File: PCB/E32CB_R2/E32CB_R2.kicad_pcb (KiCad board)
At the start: 2 copper layers, 111.3 x 90.9 mm, 89 parts, among them J1 GPIO_HEADER, J10 S, J11 Q4, J12 S, J13 Q3, J14 S, J15 Q8, J16 S, J17 Q7, J18 S, J19 Q6, J2 Power, J20 S, J21 Q5, J22 S, J3 USB_B, J4 USB +5V, J5 NEXTION, J6 I2C, J7 Q1, J8 S, J9 Q2, Q1 S8050, Q10 IRLR2905, Q2 S8050, Q3 IRLR2905, Q4 IRLR2905, Q5 IRLR2905, Q6 IRLR2905, Q7 IRLR2905, Q8 IRLR2905, Q9 IRLR2905, U1 ESP32-WROOM-32, X1 12MHz

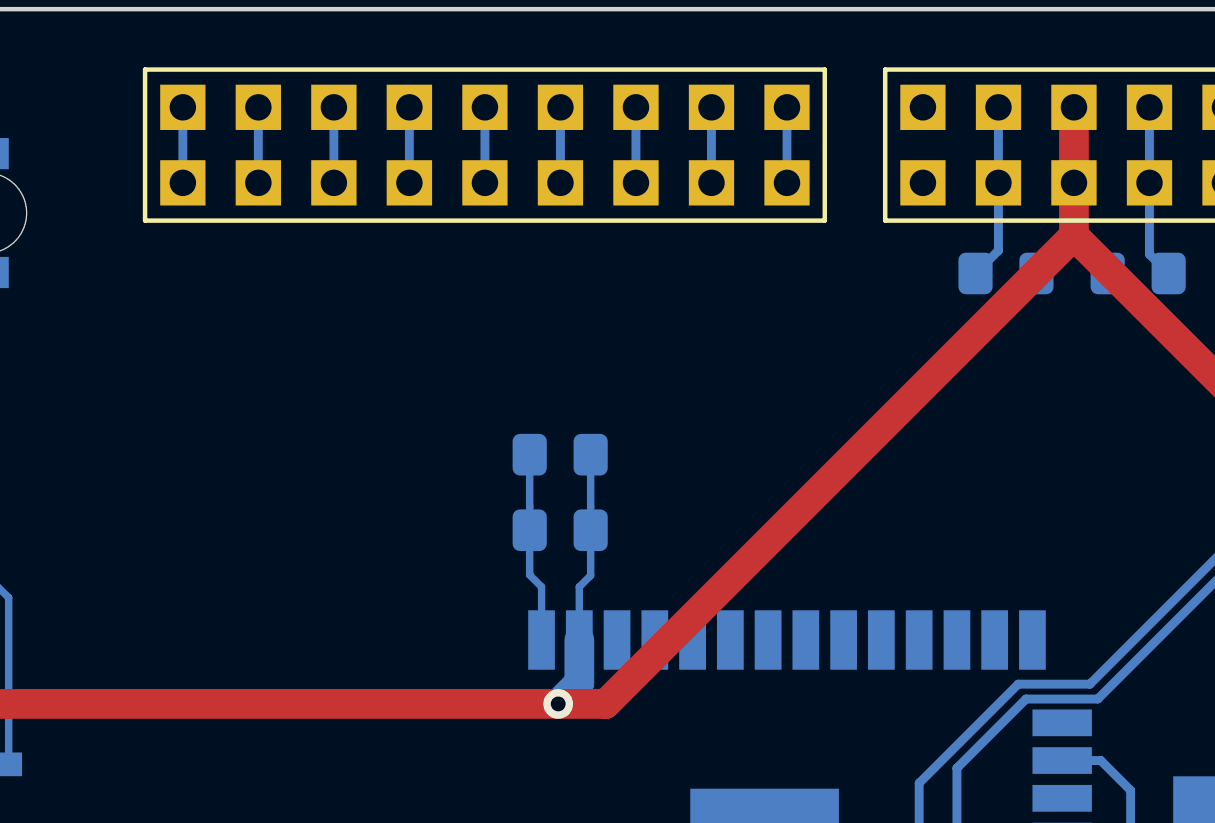
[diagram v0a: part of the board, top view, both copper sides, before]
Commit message: gpio header pins changed
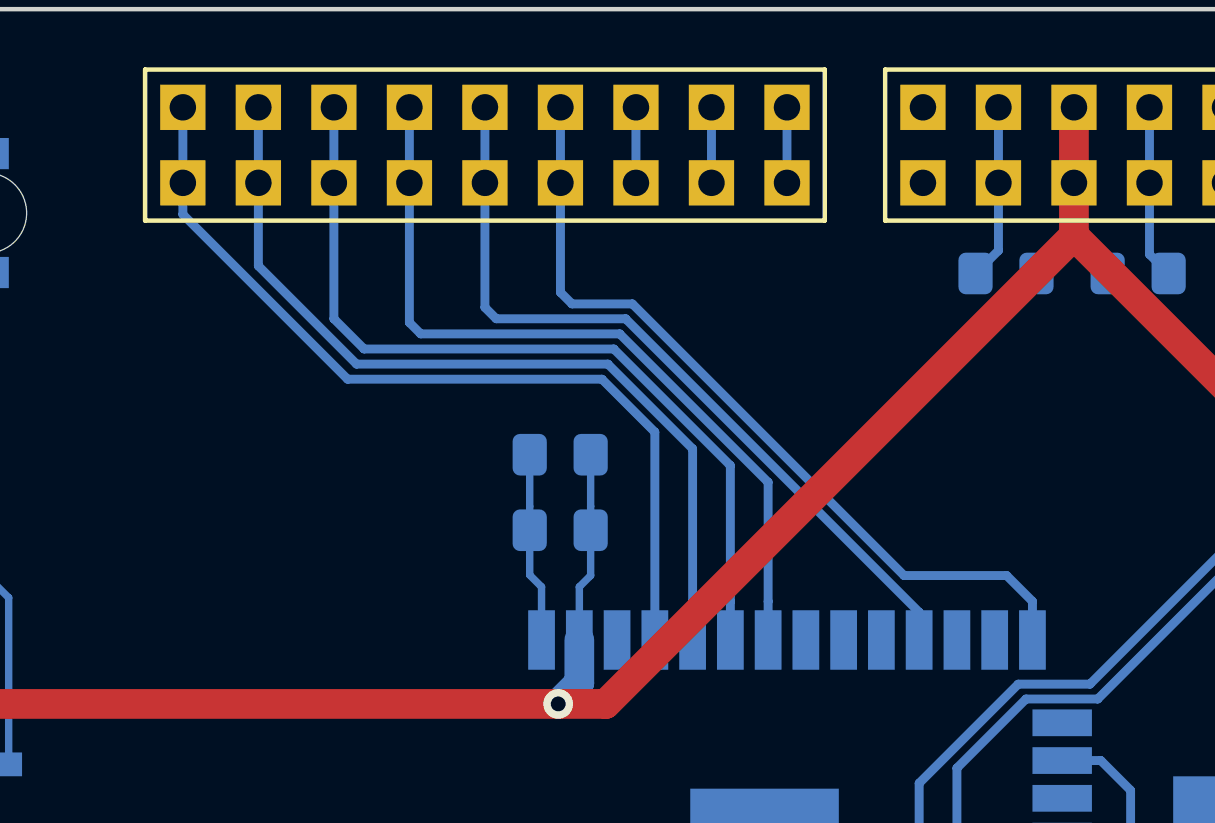
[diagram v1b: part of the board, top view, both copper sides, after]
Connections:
- J1 pad 1: /gpi39 -> /gpi36
- J1 pad 11: /gpio15 -> /gpio12
- J1 pad 12: /gpio15 -> /gpio12
- J1 pad 13: /gpio12 -> /gpio15
- J1 pad 14: /gpio12 -> /gpio15
- J1 pad 2: /gpi39 -> /gpi36
- J1 pad 3: /gpi36 -> /gpi39
- J1 pad 4: /gpi36 -> /gpi39
- J1 pad 5: /gpi35 -> /gpi34
- J1 pad 6: /gpi35 -> /gpi34
- J1 pad 7: /gpi34 -> /gpi35
- J1 pad 8: /gpi34 -> /gpi35
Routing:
- net /gpi36: track 2.54 -> 29.5 mm
- net /gpi39: track 2.54 -> 28.9 mm
- net /gpi34: track 2.54 -> 28.4 mm
- net /gpio12: track 2.54 -> 27.7 mm
- net /gpi35: track 2.54 -> 26.8 mm
- net /gpio26: track 2.54 -> 26.5 mm
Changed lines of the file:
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@@
     (thickness 1.6)
     (drawings 8)
-    (tracks 533)
+    (tracks 568)
     (zones 0)
     (modules 89)
@@
     (fp_line (start -2.54 11.43) (end -2.54 -11.43) (layer F.SilkS) (width 0.15))
     (pad 1 thru_hole rect (at -1.27 -10.16 90) (size 1.524 1.524) (drill 0.889) (layers *.Cu *.Mask F.SilkS)
-      (net 45 /gpi39))
+      (net 44 /gpi36))
     (pad 2 thru_hole rect (at 1.27 -10.16 90) (size 1.524 1.524) (drill 0.889) (layers *.Cu *.Mask F.SilkS)
-      (net 45 /gpi39))
-    (pad 3 thru_hole rect (at -1.27 -7.62 90) (size 1.524 1.524) (drill 0.889) (layers *.Cu *.Mask F.SilkS)
       (net 44 /gpi36))
+    (pad 3 thru_hole rect (at -1.27 -7.62 90) (size 1.524 1.524) (drill 0.889) (layers *.Cu *.Mask F.SilkS)
+      (net 45 /gpi39))
     (pad 4 thru_hole rect (at 1.27 -7.62 90) (size 1.524 1.524) (drill 0.889) (layers *.Cu *.Mask F.SilkS)
-      (net 44 /gpi36))
+      (net 45 /gpi39))
     (pad 5 thru_hole rect (at -1.27 -5.08 90) (size 1.524 1.524) (drill 0.889) (layers *.Cu *.Mask F.SilkS)
-      (net 47 /gpi35))
+      (net 46 /gpi34))
     (pad 6 thru_hole rect (at 1.27 -5.08 90) (size 1.524 1.524) (drill 0.889) (layers *.Cu *.Mask F.SilkS)
-      (net 47 /gpi35))
-    (pad 7 thru_hole rect (at -1.27 -2.54 90) (size 1.524 1.524) (drill 0.889) (layers *.Cu *.Mask F.SilkS)
       (net 46 /gpi34))
+    (pad 7 thru_hole rect (at -1.27 -2.54 90) (size 1.524 1.524) (drill 0.889) (layers *.Cu *.Mask F.SilkS)
+      (net 47 /gpi35))
     (pad 8 thru_hole rect (at 1.27 -2.54 90) (size 1.524 1.524) (drill 0.889) (layers *.Cu *.Mask F.SilkS)
-      (net 46 /gpi34))
+      (net 47 /gpi35))
     (pad 9 thru_hole rect (at -1.27 0 90) (size 1.524 1.524) (drill 0.889) (layers *.Cu *.Mask F.SilkS)
       (net 48 /gpio26))
@@
       (net 48 /gpio26))
     (pad 11 thru_hole rect (at -1.27 2.54 90) (size 1.524 1.524) (drill 0.889) (layers *.Cu *.Mask F.SilkS)
-      (net 56 /gpio15))
+      (net 49 /gpio12))
     (pad 12 thru_hole rect (at 1.27 2.54 90) (size 1.524 1.524) (drill 0.889) (layers *.Cu *.Mask F.SilkS)
-      (net 56 /gpio15))
-    (pad 13 thru_hole rect (at -1.27 5.08 90) (size 1.524 1.524) (drill 0.889) (layers *.Cu *.Mask F.SilkS)
       (net 49 /gpio12))
+    (pad 13 thru_hole rect (at -1.27 5.08 90) (size 1.524 1.524) (drill 0.889) (layers *.Cu *.Mask F.SilkS)
+      (net 56 /gpio15))
     (pad 14 thru_hole rect (at 1.27 5.08 90) (size 1.524 1.524) (drill 0.889) (layers *.Cu *.Mask F.SilkS)
-      (net 49 /gpio12))
+      (net 56 /gpio15))
     (pad 15 thru_hole rect (at -1.27 7.62 90) (size 1.524 1.524) (drill 0.889) (layers *.Cu *.Mask F.SilkS)
       (net 60 /gpio5))
@@
   (segment (start 119.126 115.872) (end 119.629 115.369) (width 3.7) (layer F.Cu) (net 43))
   (via (at 119.126 115.872) (size 1) (drill 0.5) (layers F.Cu B.Cu) (net 43))
-  (segment (start 132.08 49.276) (end 132.08 51.816) (width 0.3) (layer B.Cu) (net 44))
-  (segment (start 129.54 49.276) (end 129.54 51.816) (width 0.3) (layer B.Cu) (net 45))
-  (segment (start 137.16 49.276) (end 137.16 51.816) (width 0.3) (layer B.Cu) (net 46))
-  (segment (start 134.62 49.276) (end 134.62 51.816) (width 0.3) (layer B.Cu) (net 47))
+  (segment (start 132.08 49.276) (end 132.08 51.816) (width 0.3) (layer B.Cu) (net 45))
+  (segment (start 129.54 49.276) (end 129.54 51.816) (width 0.3) (layer B.Cu) (net 44))
+  (segment (start 129.54 52.878) (end 135.082 58.42) (width 0.3) (layer B.Cu) (net 44))
+  (segment (start 129.54 51.816) (end 129.54 52.878) (width 0.3) (layer B.Cu) (net 44))
+  (segment (start 135.082 58.42) (end 143.637 58.42) (width 0.3) (layer B.Cu) (net 44))
+  (segment (start 145.415 60.198) (end 145.415 67.192) (width 0.3) (layer B.Cu) (net 44))
+  (segment (start 143.637 58.42) (end 145.415 60.198) (width 0.3) (layer B.Cu) (net 44))
+  (segment (start 146.685 65.892) (end 146.685 67.192) (width 0.3) (layer B.Cu) (net 45))
+  (segment (start 146.685 60.76088) (end 146.685 65.892) (width 0.3) (layer B.Cu) (net 45))
+  (segment (start 143.83612 57.912) (end 146.685 60.76088) (width 0.3) (layer B.Cu) (net 45))
+  (segment (start 135.382 57.912) (end 143.83612 57.912) (width 0.3) (layer B.Cu) (net 45))
+  (segment (start 132.08 54.61) (end 135.382 57.912) (width 0.3) (layer B.Cu) (net 45))
+  (segment (start 132.08 51.816) (end 132.08 54.61) (width 0.3) (layer B.Cu) (net 45))
+  (segment (start 137.16 49.276) (end 137.16 51.816) (width 0.3) (layer B.Cu) (net 47))
+  (segment (start 134.62 49.276) (end 134.62 51.816) (width 0.3) (layer B.Cu) (net 46))
+  (segment (start 147.955 65.892) (end 147.955 67.192) (width 0.3) (layer B.Cu) (net 46))
+  (segment (start 147.955 61.32376) (end 147.955 65.892) (width 0.3) (layer B.Cu) (net 46))
+  (segment (start 144.03524 57.404) (end 147.955 61.32376) (width 0.3) (layer B.Cu) (net 46))
+  (segment (start 135.636 57.404) (end 144.03524 57.404) (width 0.3) (layer B.Cu) (net 46))
+  (segment (start 134.62 56.388) (end 135.636 57.404) (width 0.3) (layer B.Cu) (net 46))
+  (segment (start 134.62 51.816) (end 134.62 56.388) (width 0.3) (layer B.Cu) (net 46))
+  (segment (start 149.225 65.892) (end 149.225 67.192) (width 0.3) (layer B.Cu) (net 47))
+  (segment (start 149.225 61.88664) (end 149.225 65.892) (width 0.3) (layer B.Cu) (net 47))
+  (segment (start 144.23436 56.896) (end 149.225 61.88664) (width 0.3) (layer B.Cu) (net 47))
+  (segment (start 137.16 51.816) (end 137.16 56.515) (width 0.3) (layer B.Cu) (net 47))
+  (segment (start 137.541 56.896) (end 144.23436 56.896) (width 0.3) (layer B.Cu) (net 47))
+  (segment (start 137.16 56.515) (end 137.541 56.896) (width 0.3) (layer B.Cu) (net 47))
   (segment (start 139.7 49.276) (end 139.7 51.816) (width 0.3) (layer B.Cu) (net 48))
-  (segment (start 144.78 49.276) (end 144.78 51.816) (width 0.3) (layer B.Cu) (net 49))
-  (segment (start 142.24 49.276) (end 142.24 51.816) (width 0.3) (layer B.Cu) (net 56))
+  (segment (start 154.305 66.25952) (end 154.305 67.192) (width 0.3) (layer B.Cu) (net 48))
+  (segment (start 144.43348 56.388) (end 154.305 66.25952) (width 0.3) (layer B.Cu) (net 48))
+  (segment (start 140.081 56.388) (end 144.43348 56.388) (width 0.3) (layer B.Cu) (net 48))
+  (segment (start 139.7 51.816) (end 139.7 56.007) (width 0.3) (layer B.Cu) (net 48))
+  (segment (start 139.7 56.007) (end 140.081 56.388) (width 0.3) (layer B.Cu) (net 48))
+  (segment (start 144.78 49.276) (end 144.78 51.816) (width 0.3) (layer B.Cu) (net 56))
+  (segment (start 142.24 49.276) (end 142.24 51.816) (width 0.3) (layer B.Cu) (net 49))
+  (segment (start 158.115 65.892) (end 158.115 67.192) (width 0.3) (layer B.Cu) (net 49))
+  (segment (start 142.24 51.816) (end 142.24 55.499) (width 0.3) (layer B.Cu) (net 49))
+  (segment (start 142.24 55.499) (end 142.62899 55.88799) (width 0.3) (layer B.Cu) (net 49))
+  (segment (start 142.62899 55.88799) (end 144.66099 55.88799) (width 0.3) (layer B.Cu) (net 49))
+  (segment (start 153.797 65.024) (end 157.247 65.024) (width 0.3) (layer B.Cu) (net 49))
+  (segment (start 144.66099 55.88799) (end 153.797 65.024) (width 0.3) (layer B.Cu) (net 49))
+  (segment (start 157.247 65.024) (end 158.115 65.892) (width 0.3) (layer B.Cu) (net 49))
   (segment (start 149.86 49.276) (end 149.86 51.816) (width 0.3) (layer B.Cu) (net 57))
   (segment (start 155.575 71.501) (end 155.575 84.192) (width 0.3) (layer B.Cu) (net 58))

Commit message: gpio chenged
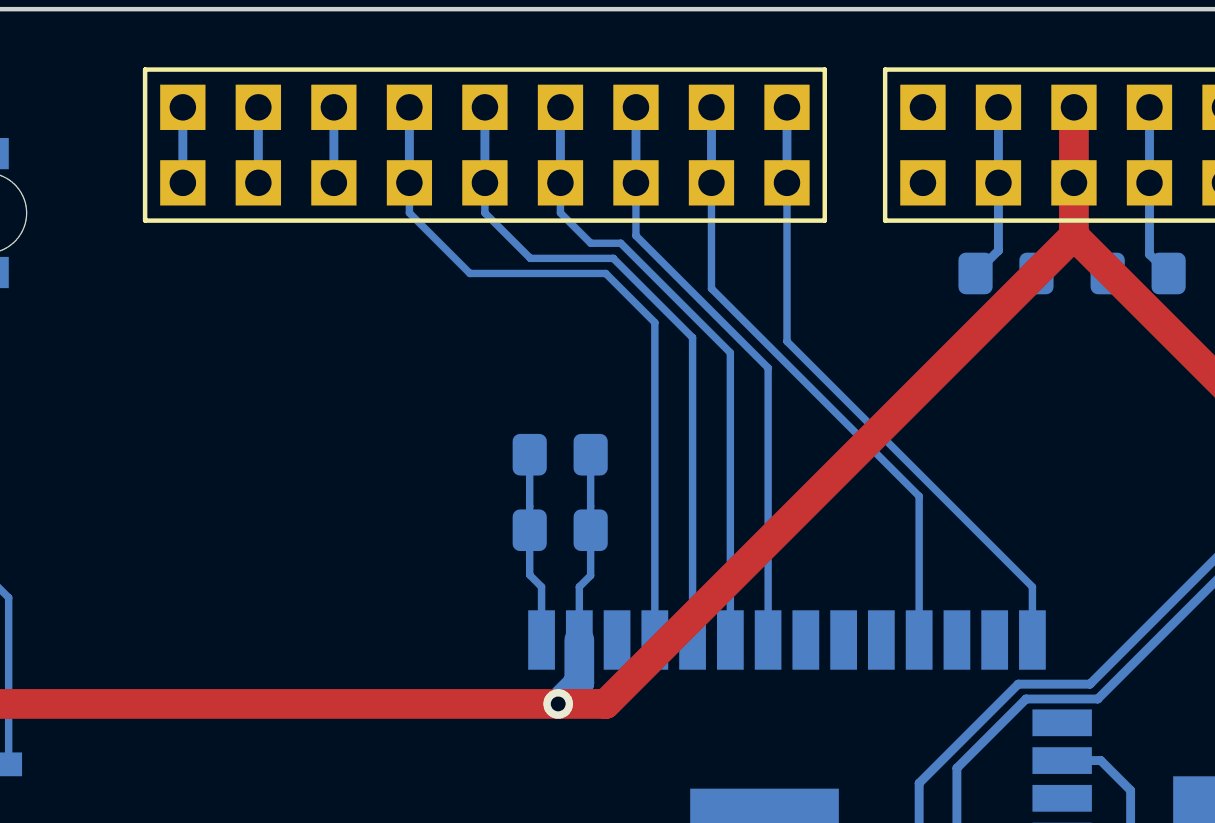
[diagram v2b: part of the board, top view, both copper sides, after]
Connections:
- J1 pad 1: /gpi36 -> /gpio15
- J1 pad 10: /gpio26 -> /gpi39
- J1 pad 11: /gpio12 -> /gpi34
- J1 pad 12: /gpio12 -> /gpi34
- J1 pad 13: /gpio15 -> /gpi35
- J1 pad 14: /gpio15 -> /gpi35
- J1 pad 15: /gpio5 -> /gpio26
- J1 pad 16: /gpio5 -> /gpio26
- J1 pad 17: /gpio2 -> /gpio12
- J1 pad 18: /gpio2 -> /gpio12
- J1 pad 2: /gpi36 -> /gpio15
- J1 pad 3: /gpi39 -> /gpio5
- J1 pad 4: /gpi39 -> /gpio5
- J1 pad 5: /gpi34 -> /gpio2
- J1 pad 6: /gpi34 -> /gpio2
- J1 pad 7: /gpi35 -> /gpi36
- J1 pad 8: /gpi35 -> /gpi36
- J1 pad 9: /gpio26 -> /gpi39
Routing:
- net /gpi34: track 28.4 -> 20.9 mm
- net /gpi35: track 26.8 -> 19.8 mm
- net /gpi39: track 28.9 -> 22.4 mm
- net /gpio12: track 27.7 -> 21.3 mm
- net /gpio26: track 26.5 -> 20.8 mm
- net /gpi36: track 29.5 -> 24.0 mm

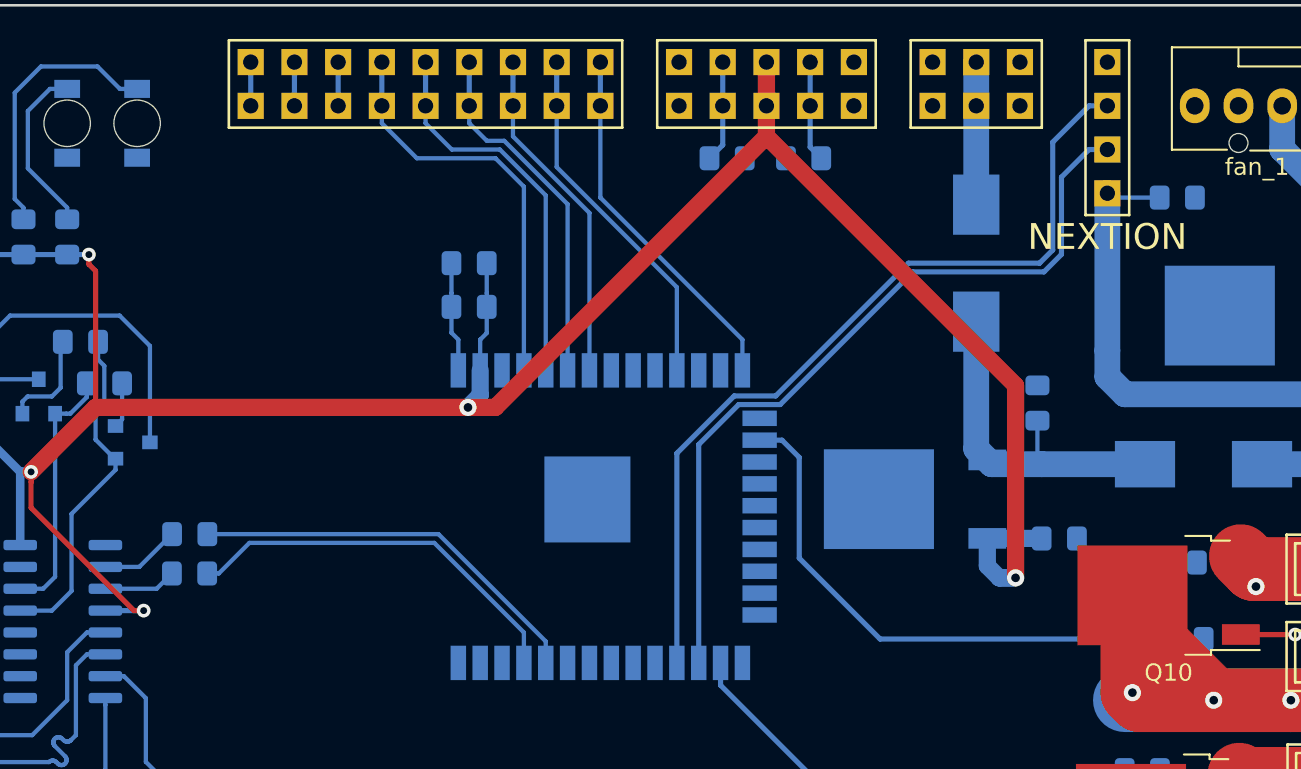
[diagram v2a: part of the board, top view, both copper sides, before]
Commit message: gpio connected
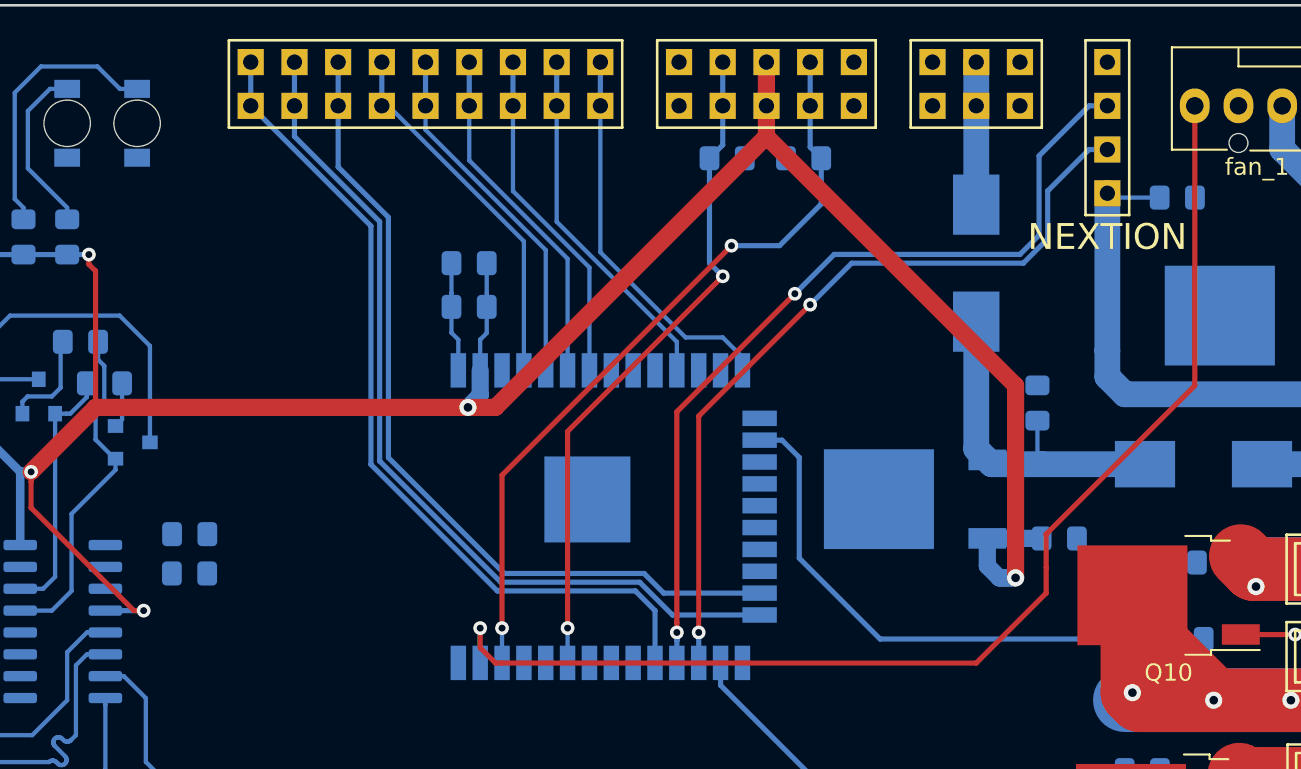
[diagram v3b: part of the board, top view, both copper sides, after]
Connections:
- J1 pad 1: /gpio15 -> /gpio5
- J1 pad 2: /gpio15 -> /gpio5
- J1 pad 3: /gpio5 -> /gpio2
- J1 pad 4: /gpio5 -> /gpio2
- J1 pad 5: /gpio2 -> /gpio15
- J1 pad 6: /gpio2 -> /gpio15
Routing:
- net /fan1: track 0.00 -> 70.0 mm, vias 0 -> 1
- net /gpio2: track 2.54 -> 51.0 mm
- net /gpio5: track 2.54 -> 49.3 mm
- net /gpio15: track 2.54 -> 49.0 mm
- net /I2C_SCL: track 5.85 -> 44.5 mm, vias 0 -> 2
- net /I2C_SDA: track 5.91 -> 39.3 mm, vias 0 -> 2
- net /RXD: track 23.5 -> 0.00 mm
- net /TXD: track 23.1 -> 0.00 mm
- net Net-(CH340G1-Pad2): track 4.66 -> 0.00 mm
- net Net-(CH340G1-Pad3): track 4.23 -> 0.00 mm
- net /gpi36: track 24.0 -> 21.6 mm
- net /gpi39: track 22.4 -> 20.8 mm
- net /U2_TXD: track 49.2 -> 50.6 mm, vias 0 -> 2
- net /gpio12: track 21.3 -> 22.6 mm
- net /gpi34: track 20.9 -> 20.3 mm
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
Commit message: update
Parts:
- moved C8 6.65 mm to (168.7, 68.3), turned to 180 degrees
- moved C9 4.83 mm to (181.4, 77.2)
- moved 3V3stabilizer1 3.69 mm to (171.8, 74.8)
- moved R24 2.65 mm to (181.4, 82.0)
- moved R28 2.50 mm to (181.4, 79.6)
- moved R7 1.28 mm to (124.7, 76.7)
- moved R8 0.80 mm to (126.7, 79.2)
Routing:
- net +3V3: track 153.2 -> 78.6 mm, vias 5 -> 0
- net /RXD: track 0.00 -> 53.4 mm
- net /TXD: track 0.00 -> 48.2 mm
- net /s_LED: track 0.00 -> 47.8 mm, vias 0 -> 2
- net /Q5: track 32.0 -> 0.00 mm
- net Net-(CH340G1-Pad3): track 0.00 -> 4.89 mm
- net Net-(3V3stabilizer1-Pad1): track 20.2 -> 15.5 mm
- net Net-(CH340G1-Pad2): track 0.00 -> 4.13 mm
- net /fan1: track 70.0 -> 67.3 mm, vias 1 -> 2
- net /I2C_SCL: track 44.5 -> 45.8 mm
- net /I2C_SDA: track 39.3 -> 38.7 mm
- net /U2_RXD: track 46.1 -> 46.8 mm
- net /U2_TXD: track 50.6 -> 51.2 mm

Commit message: pcb update
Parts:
- moved C6 6.91 mm to (189.0, 57.4), turned to 180 degrees
- moved RESET1 3.59 mm to (100.5, 73.4)
- moved FLASH1 3.59 mm to (107.0, 68.3)
- moved fan_1 2.54 mm to (194.6, 51.8)
- moved F1 1.44 mm to (103.6, 105.2), turned to 180 degrees
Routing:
- net +3V3: track 78.6 -> 111.2 mm
- net /Q6: track 30.1 -> 0.00 mm
- net Net-(C3-Pad1): track 14.1 -> 0.00 mm
- net Net-(J22-Pad1): track 29.8 -> 35.7 mm
- net /EN: track 17.1 -> 20.0 mm
- net /fan1: track 67.3 -> 69.9 mm
- net /IO_0: track 32.4 -> 30.9 mm
- net +12V: track 52.1 -> 50.9 mm

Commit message: update
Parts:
- moved F1 9.26 mm to (112.0, 101.2), turned to 90 degrees
- moved C3 3.30 mm to (116.6, 98.9)
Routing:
- net +5V: track 8.28 -> 118.0 mm, vias 0 -> 2
- net +3V3: track 111.2 -> 176.0 mm, vias 0 -> 2
- net /s_LED: track 47.8 -> 25.4 mm, vias 2 -> 0
- net Net-(C3-Pad1): track 0.00 -> 10.2 mm
